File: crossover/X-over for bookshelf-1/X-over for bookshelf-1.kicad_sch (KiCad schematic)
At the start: 10 parts, among them J1 Screw_Terminal_01x02, J2 Screw_Terminal_01x04

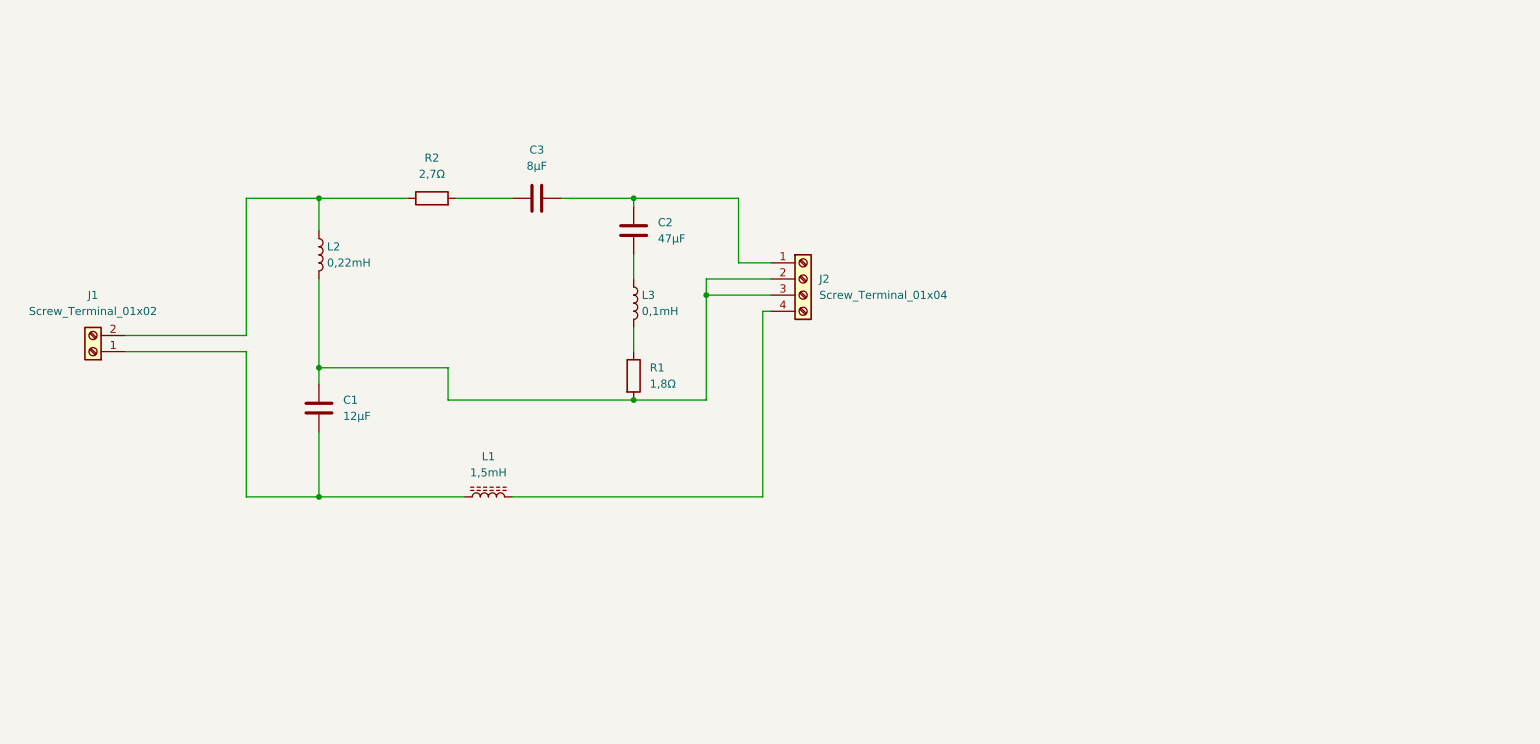
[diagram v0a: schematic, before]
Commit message: Updated schematic and board layout, according to PdB Spec (#4)
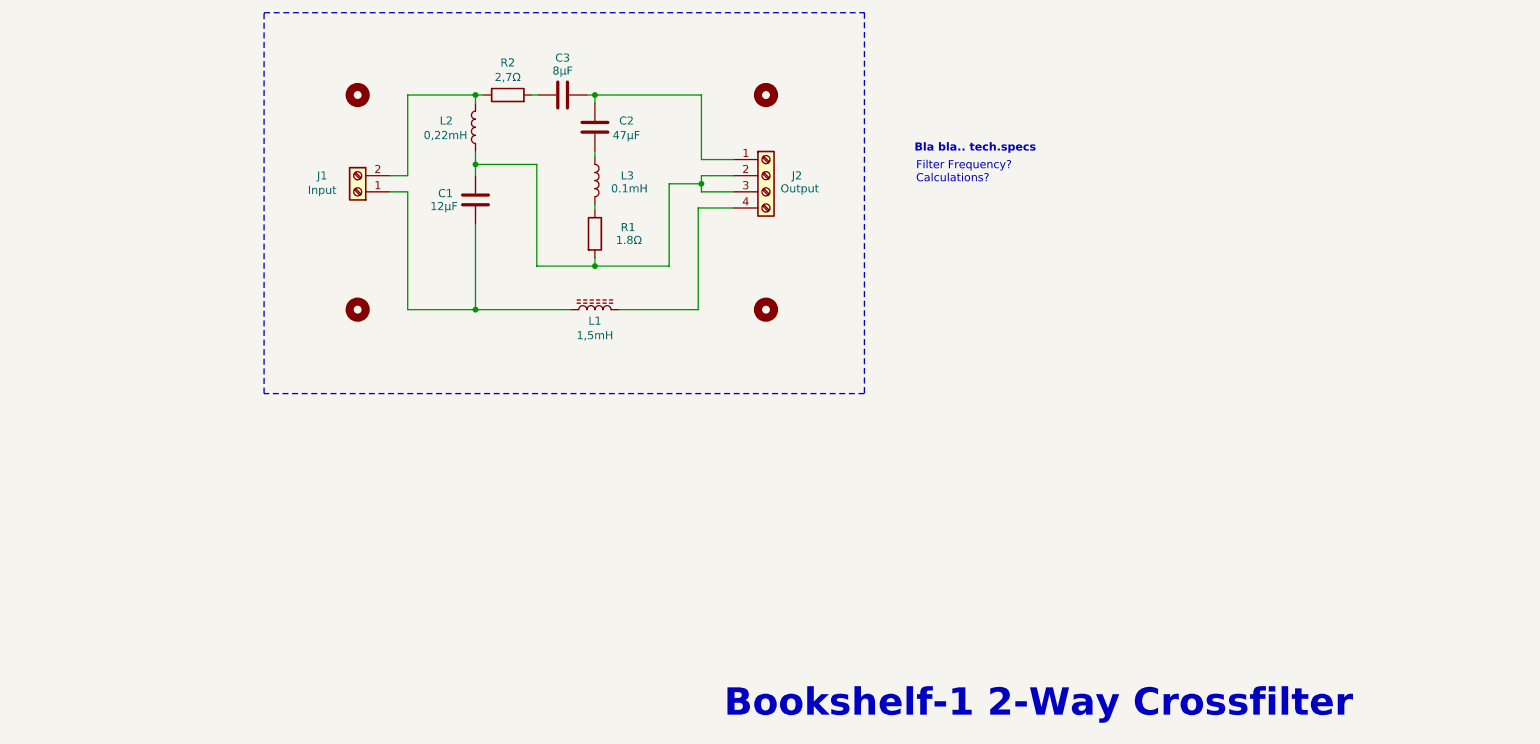
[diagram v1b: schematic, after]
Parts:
- added H1, H2, H3, H4: MountingHole, MountingHole:MountingHole_4.3mm_M4_DIN965_Pad, symbol Mechanical:MountingHole
- J1: value Screw_Terminal_01x02 -> Input
- J2: value Screw_Terminal_01x04 -> Output
- L3: value 0,1mH -> 0.1mH
- R1: value 1,8Ω -> 1.8Ω
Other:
- note added: "Bla bla.. tech.specs"
- note added: "Bookshelf-1 2-Way Crossfilter"
- note added: "Filter Frequency? Calculations?"
- moved on the sheet: C1, C2, C3, J1, J2, L1, L2, L3, R1, R2
